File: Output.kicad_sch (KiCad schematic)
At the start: 15 parts, among them U401 74ACT157

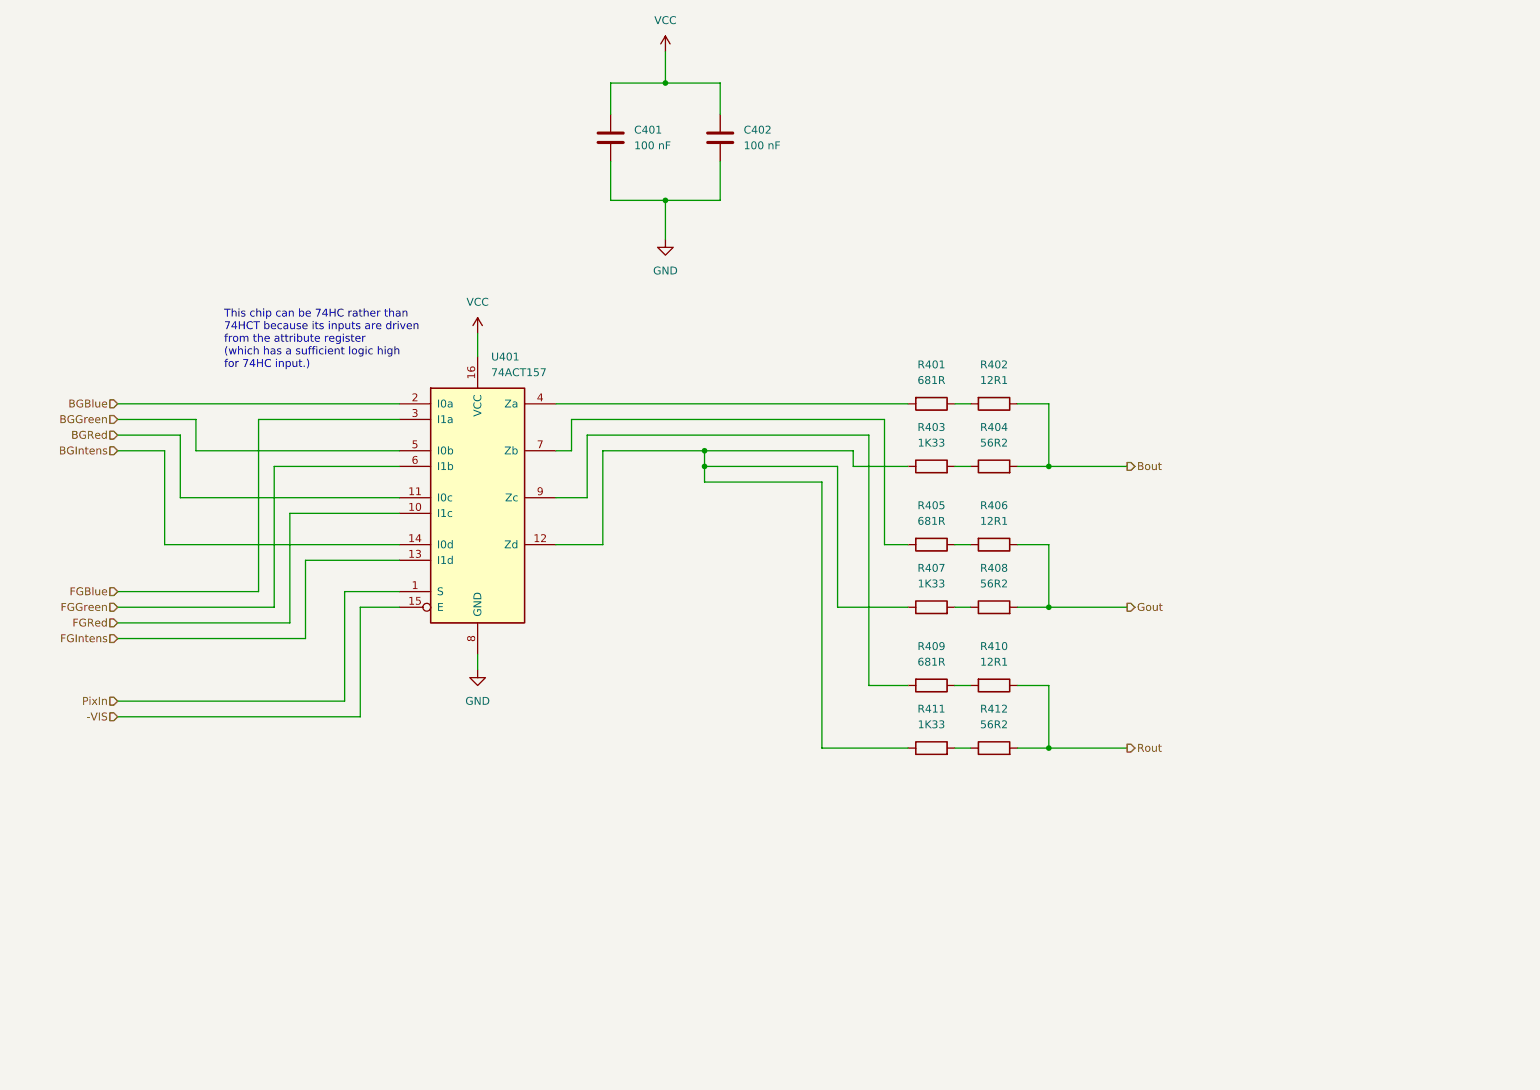
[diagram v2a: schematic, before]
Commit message: minor tweaks to Output circuit
The multiplexor definitely needs to be 74ACT.

Tweaked DAC resistor values to be ones that are more likely
I actually have. (I don't have any 1.33K, for example.)
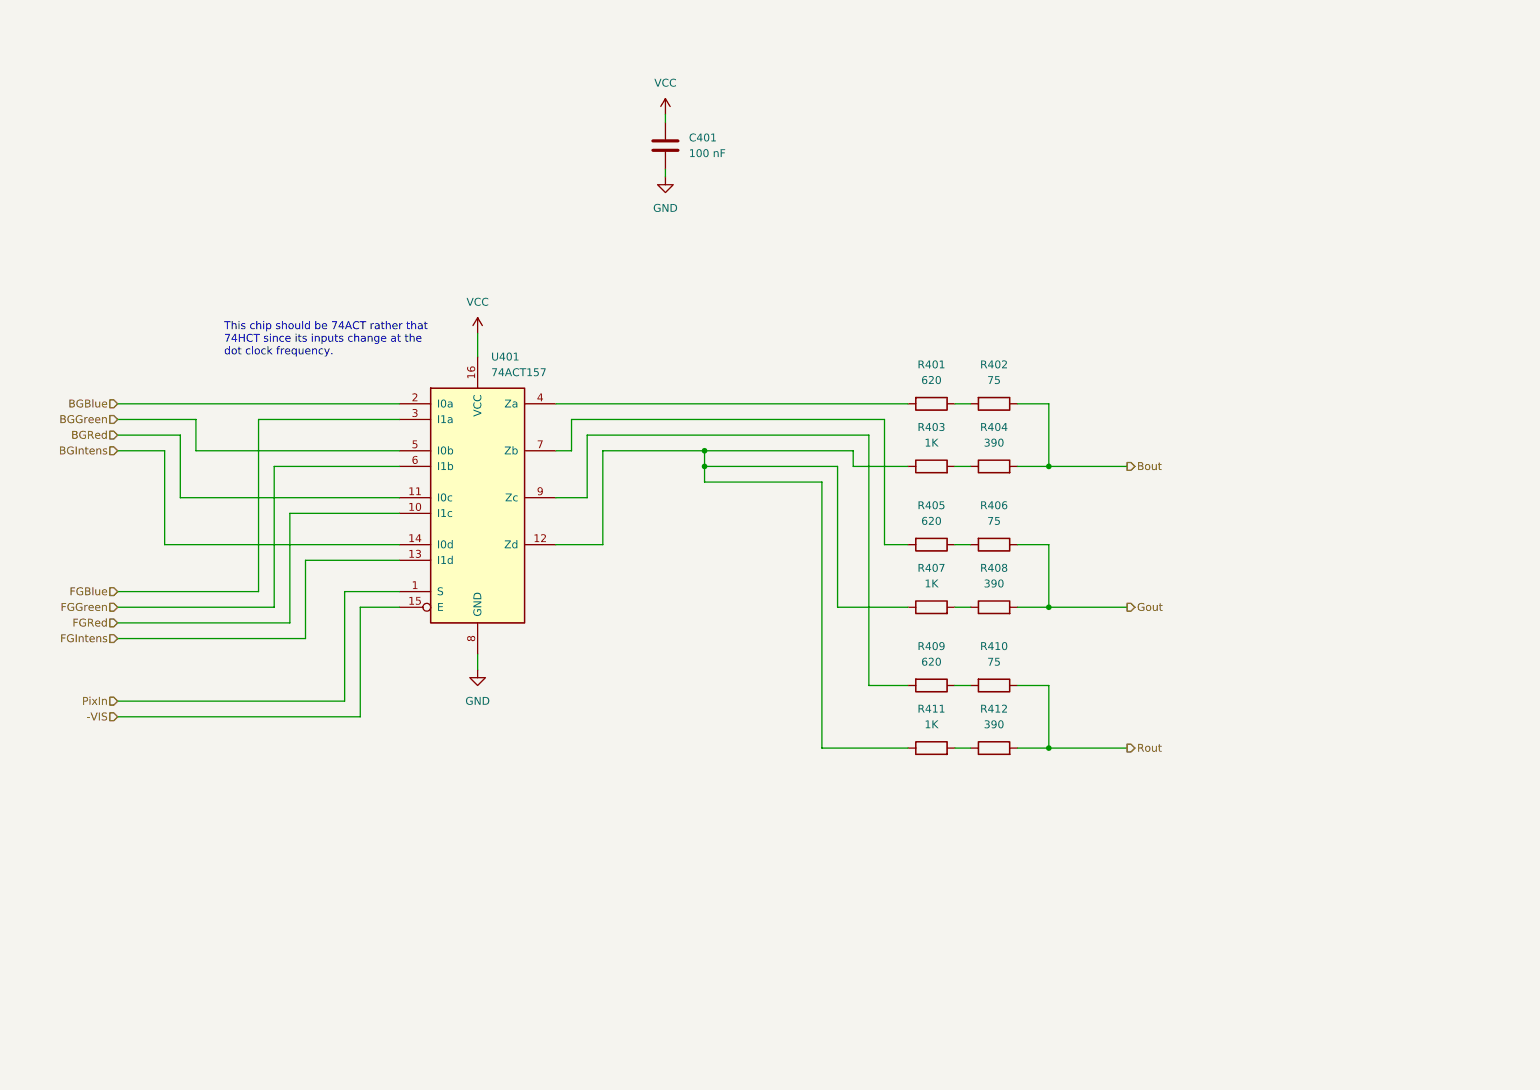
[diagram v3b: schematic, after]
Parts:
- removed C402: 100 nF, symbol Device:C
- R401, R405, R409: value 681R -> 620
- R402, R406, R410: value 12R1 -> 75
- R403, R407, R411: value 1K33 -> 1K
- R404, R408, R412: value 56R2 -> 390
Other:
- note added: "This chip should be 74ACT rather that 74HCT since its inputs change at the dot clock frequency."
- note removed: "This chip can be 74HC rather than 74HCT because its inputs are driven from the attribute register (which has a sufficient logic high for 74HC input.)"
- moved on the sheet: C401
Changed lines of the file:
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@@
-	)
-	(junction
-		(at 128.27 29.21)
-		(diameter 0)
-		(color 0 0 0 0)
 	)
 	(junction
@@
 	)
 	(junction
-		(at 128.27 48.26)
-		(diameter 0)
-		(color 0 0 0 0)
-	)
-	(junction
 		(at 134.62 88.9)
 		(diameter 0)
@@
 	(wire
 		(pts
-			(xy 119.38 41.91) (xy 119.38 48.26)
+			(xy 128.27 43.18) (xy 128.27 44.45)
 		)
 		(stroke
@@
 	(wire
 		(pts
-			(xy 128.27 48.26) (xy 128.27 54.61)
-		)
-		(stroke
-			(width 0)
-			(type default)
-		)
-	)
-	(wire
-		(pts
 			(xy 49.53 86.36) (xy 49.53 96.52)
 		)
@@
 	(wire
 		(pts
-			(xy 128.27 24.13) (xy 128.27 29.21)
-		)
-		(stroke
-			(width 0)
-			(type default)
-		)
-	)
-	(wire
-		(pts
 			(xy 113.03 88.9) (xy 113.03 83.82)
 		)
@@
 	(wire
 		(pts
-			(xy 137.16 29.21) (xy 137.16 34.29)
-		)
-		(stroke
-			(width 0)
-			(type default)
-		)
-	)
-	(wire
-		(pts
-			(xy 119.38 48.26) (xy 128.27 48.26)
-		)
-		(stroke
-			(width 0)
-			(type default)
-		)
-	)
-	(wire
-		(pts
 			(xy 39.37 86.36) (xy 49.53 86.36)
 		)
@@
 	(wire
 		(pts
-			(xy 119.38 29.21) (xy 128.27 29.21)
-		)
-		(stroke
-			(width 0)
-			(type default)
-		)
-	)
-	(wire
-		(pts
 			(xy 156.21 114.3) (xy 156.21 91.44)
 		)
@@
 	(wire
 		(pts
-			(xy 128.27 29.21) (xy 137.16 29.21)
-		)
-		(stroke
-			(width 0)
-			(type default)
-		)
-	)
-	(wire
-		(pts
 			(xy 64.77 114.3) (xy 64.77 91.44)
 		)
@@
 	(wire
 		(pts
-			(xy 128.27 48.26) (xy 137.16 48.26)
-		)
-		(stroke
-			(width 0)
-			(type default)
-		)
-	)
-	(wire
-		(pts
 			(xy 167.64 114.3) (xy 156.21 114.3)
 		)
@@
 	(wire
 		(pts
-			(xy 137.16 48.26) (xy 137.16 41.91)
-		)
-		(stroke
-			(width 0)
-			(type default)
-		)
-	)
-	(wire
-		(pts
-			(xy 119.38 34.29) (xy 119.38 29.21)
+			(xy 128.27 34.29) (xy 128.27 35.56)
 		)
 		(stroke
@@
 		)
 	)
-	(text "This chip can be 74HC rather than\n74HCT because its inputs are driven\nfrom the attribute register\n(which has a sufficient logic high\nfor 74HC input.)"
+	(text "This chip should be 74ACT rather that\n74HCT since its inputs change at the\ndot clock frequency."
 		(exclude_from_sim no)
 		(at 56.642 70.866 0)
@@
 			)
 		)
-		(property "Value" "681R"
+		(property "Value" "620"
 			(at 171.45 100.33 90)
 			(effects
@@
 			)
 		)
-		(property "Value" "1K33"
+		(property "Value" "1K"
 			(at 171.45 110.49 90)
 			(effects
@@
 	(symbol
 		(lib_id "power:GND")
-		(at 128.27 54.61 0)
+		(at 128.27 44.45 0)
 		(unit 1)
 		(exclude_from_sim no)
@@
 		(fields_autoplaced yes)
 		(property "Reference" "#PWR046"
-			(at 128.27 60.96 0)
+			(at 128.27 50.8 0)
 			(effects
 				(font
@@
 		)
 		(property "Value" "GND"
-			(at 128.27 59.69 0)
+			(at 128.27 49.53 0)
 			(effects
 				(font
@@
 		)
 		(property "Footprint" ""
-			(at 128.27 54.61 0)
+			(at 128.27 44.45 0)
 			(effects
 				(font
@@
 		)
 		(property "Datasheet" ""
-			(at 128.27 54.61 0)
+			(at 128.27 44.45 0)
 			(effects
 				(font
@@
 		)
 		(property "Description" "Power symbol creates a global label with name \"GND\" , ground"
-			(at 128.27 54.61 0)
+			(at 128.27 44.45 0)
 			(effects
 				(font
@@
 			)
 		)
-		(property "Value" "1K33"
+		(property "Value" "1K"
 			(at 171.45 87.63 90)
 			(effects
@@
 			)
 		)
-		(property "Value" "56R2"
+		(property "Value" "390"
 			(at 181.61 110.49 90)
 			(effects
@@
 			)
 		)
-		(property "Value" "681R"
+		(property "Value" "620"
 			(at 171.45 77.47 90)
 			(effects
@@
 	(symbol
 		(lib_id "power:VCC")
-		(at 128.27 24.13 0)
+		(at 128.27 34.29 0)
 		(unit 1)
 		(exclude_from_sim no)
@@
 		(fields_autoplaced yes)
 		(property "Reference" "#PWR045"
-			(at 128.27 27.94 0)
+			(at 128.27 38.1 0)
 			(effects
 				(font
@@
 		)
 		(property "Value" "VCC"
-			(at 128.27 19.05 0)
+			(at 128.27 29.21 0)
 			(effects
 				(font
@@
 		)
 		(property "Footprint" ""
-			(at 128.27 24.13 0)
+			(at 128.27 34.29 0)
 			(effects
 				(font
@@
 		)
 		(property "Datasheet" ""
-			(at 128.27 24.13 0)
+			(at 128.27 34.29 0)
 			(effects
 				(font
@@
 		)
 		(property "Description" "Power symbol creates a global label with name \"VCC\""
-			(at 128.27 24.13 0)
+			(at 128.27 34.29 0)
 			(effects
 				(font
@@
 			)
 		)
-		(property "Value" "12R1"
+		(property "Value" "75"
 			(at 181.61 123.19 90)
 			(effects
@@
 			)
 		)
-		(property "Value" "12R1"
+		(property "Value" "75"
 			(at 181.61 77.47 90)
 			(effects
@@
 			)
 		)
-		(property "Value" "12R1"
+		(property "Value" "75"
 			(at 181.61 100.33 90)
 			(effects
@@
 	(symbol
 		(lib_id "Device:C")
-		(at 119.38 38.1 0)
+		(at 128.27 39.37 0)
 		(unit 1)
 		(exclude_from_sim no)
@@
 		(fields_autoplaced yes)
 		(property "Reference" "C401"
-			(at 123.19 36.8299 0)
+			(at 132.08 38.0999 0)
 			(effects
 				(font
@@
 		)
 		(property "Value" "100 nF"
-			(at 123.19 39.3699 0)
+			(at 132.08 40.6399 0)
 			(effects
 				(font
@@
 		)
 		(property "Footprint" ""
-			(at 120.3452 41.91 0)
+			(at 129.2352 43.18 0)
 			(effects
 				(font
@@
 		)
 		(property "Datasheet" "~"
-			(at 119.38 38.1 0)
+			(at 128.27 39.37 0)
 			(effects
 				(font
@@
 		)
 		(property "Description" "Unpolarized capacitor"
-			(at 119.38 38.1 0)
+			(at 128.27 39.37 0)
 			(effects
 				(font
@@
 	)
 	(symbol
-		(lib_id "Device:C")
-		(at 137.16 38.1 0)
-		(unit 1)
-		(exclude_from_sim no)
-		(in_bom yes)
-		(on_board yes)
-		(dnp no)
-		(fields_autoplaced yes)
-		(property "Reference" "C402"
-			(at 140.97 36.8299 0)
-			(effects
-				(font
-					(size 1.27 1.27)
-				)
-				(justify left)
-			)
-		)
-		(property "Value" "100 nF"
-			(at 140.97 39.3699 0)
-			(effects
-				(font
-					(size 1.27 1.27)
-				)
-				(justify left)
-			)
-		)
-		(property "Footprint" ""
-			(at 138.1252 41.91 0)
-			(effects
-				(font
-					(size 1.27 1.27)
-				)
-				(hide yes)
-			)
-		)
-		(property "Datasheet" "~"
-			(at 137.16 38.1 0)
-			(effects
-				(font
-					(size 1.27 1.27)
-				)
-				(hide yes)
-			)
-		)
-		(property "Description" "Unpolarized capacitor"
-			(at 137.16 38.1 0)
-			(effects
-				(font
-					(size 1.27 1.27)
-				)
-				(hide yes)
-			)
-		)
-		(pin "2"
-		)
-		(pin "1"
-		)
-		(instances
-			(project "HW_VGA"
-				(path "/c4bd4b39-993a-4195-805f-b4de6fa4aea5/6938dbb6-3e46-4ac6-b400-805c357c7abb"
-					(reference "C402")
-					(unit 1)
-				)
-			)
-		)
-	)
-	(symbol
 		(lib_id "Device:R")
 		(at 171.45 137.16 90)
@@
 			)
 		)
-		(property "Value" "1K33"
+		(property "Value" "1K"
 			(at 171.45 133.35 90)
 			(effects
@@
 			)
 		)
-		(property "Value" "681R"
+		(property "Value" "620"
 			(at 171.45 123.19 90)
 			(effects
@@
 			)
 		)
-		(property "Value" "56R2"
+		(property "Value" "390"
 			(at 181.61 87.63 90)
 			(effects
@@
 			)
 		)
-		(property "Value" "56R2"
+		(property "Value" "390"
 			(at 181.61 133.35 90)
 			(effects

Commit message: update Output circuit to use '574 as output reg
I think it makes sense to have a register for the
color signal output.
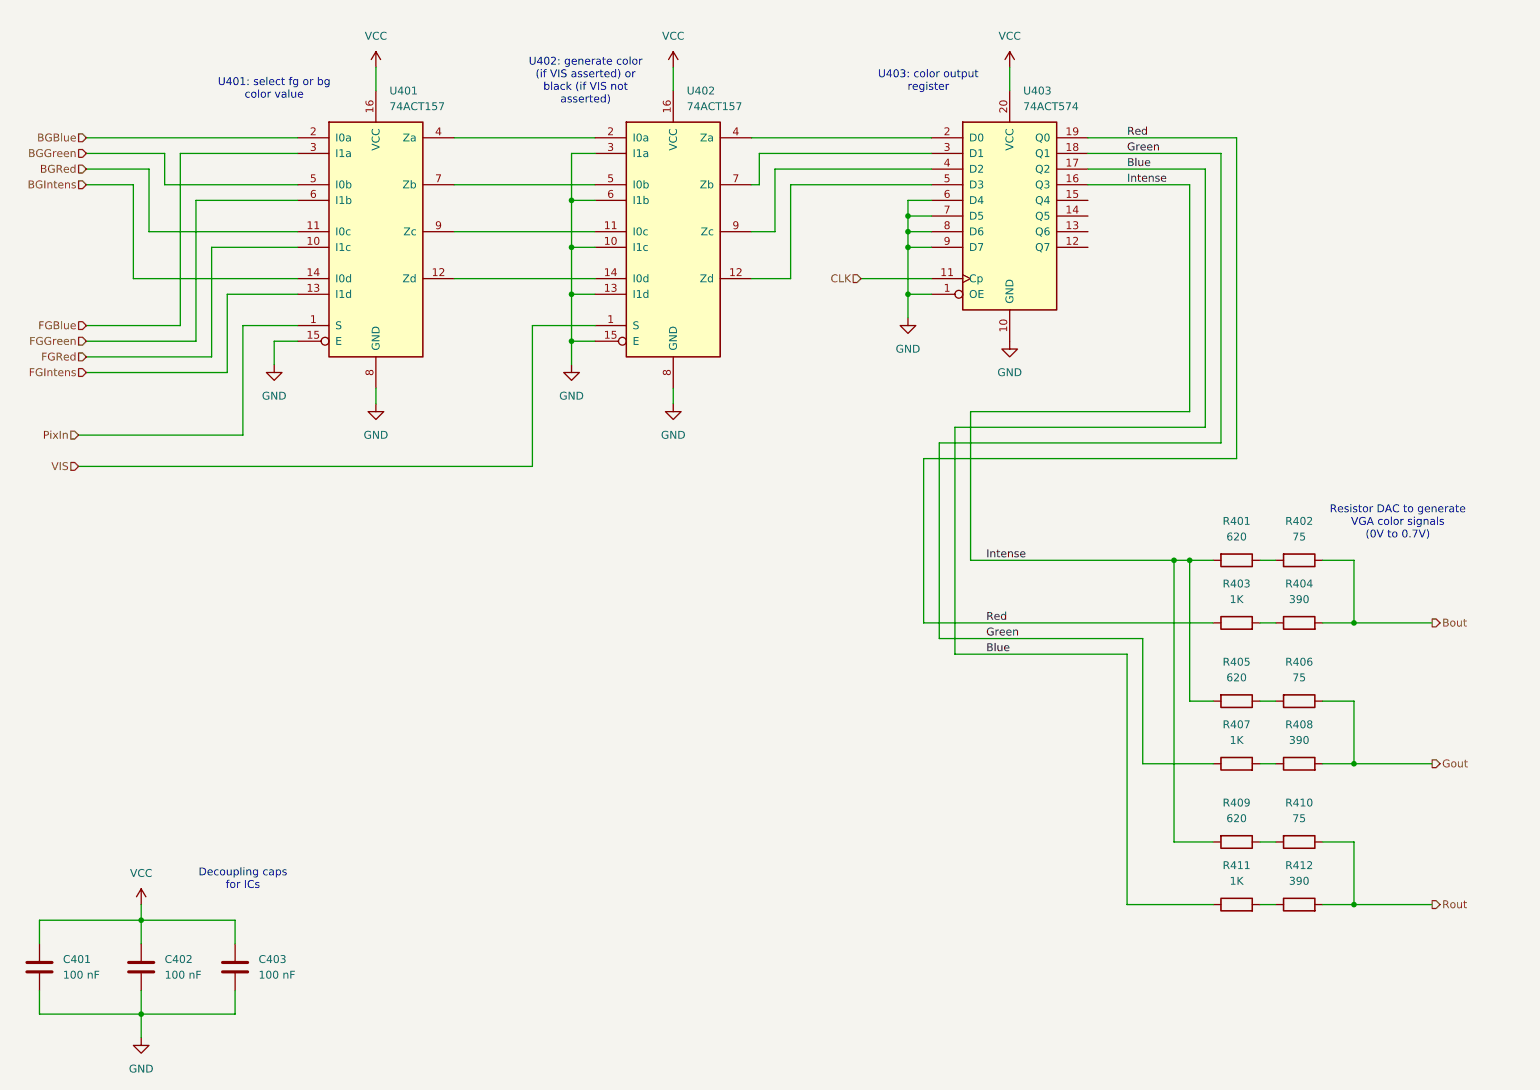
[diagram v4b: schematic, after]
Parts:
- added C402, C403: 100 nF, symbol Device:C
- added U402: 74ACT157, symbol 74xx:74LS157
- added U403: 74ACT574, symbol 74xx:74LS574
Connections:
- net -VIS is gone; now on net GND: U401.15 (E)
- net GND: now also C402.2, C403.2, U402.10 (I1c), U402.13 (I1d), U402.15 (E), U402.3 (I1a), U402.6 (I1b), U402.8 (GND), U403.1 (OE), U403.10 (GND), U403.6 (D4), U403.7 (D5), U403.8 (D6), U403.9 (D7)
- net VCC: now also C402.1, C403.1, U402.16 (VCC), U403.20 (VCC)
- net at U401.7 (Zb): now also U402.5 (I0b); no longer R405.2
- net at U401.4 (Za): now also U402.2 (I0a); no longer R401.2
- net at U401.9 (Zc): now also U402.11 (I0c); no longer R409.2
- new net: U402.4 (Za), U403.2 (D0)
- new net: U402.7 (Zb), U403.3 (D1)
- new net: U402.9 (Zc), U403.4 (D2)
- new net: U402.12 (Zd), U403.5 (D3)
- new net: U401.12 (Zd), U402.14 (I0d)
- new net Blue: R411.1, U403.17 (Q2)
- new net CLK: U403.11 (Cp)
- new net Green: R407.1, U403.18 (Q1)
- new net Intense: R401.2, R405.2, R409.2, U403.16 (Q3)
- new net Red: R403.1, U403.19 (Q0)
- new net VIS: U402.1 (S)
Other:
- note added: "Decoupling caps for ICs"
- note added: "Resistor DAC to generate VGA color signals (0V to 0.7V)"
- note added: "U401: select fg or bg color value"
- note added: "U402: generate color (if VIS asserted) or black (if VIS not asserted)"
- note added: "U403: color output register"
- note removed: "This chip should be 74ACT rather that 74HCT since its inputs change at the dot clock frequency."
- moved on the sheet: C401, R401, R402, R403, R404, R405, R406, R407, R408, R409, R410, R411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

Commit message: make -VIS active-low again
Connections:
- net VIS renamed -VIS
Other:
- note added: "U402: generate color (if -VIS asserted) or black (if -VIS not asserted)"
- note removed: "U402: generate color (if VIS asserted) or black (if VIS not asserted)"
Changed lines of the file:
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@@
 		)
 	)
-	(text "U402: generate color\n(if VIS asserted) or\nblack (if VIS not\nasserted)"
+	(text "U402: generate color\n(if -VIS asserted) or\nblack (if -VIS not\nasserted)"
 		(exclude_from_sim no)
 		(at 115.316 28.956 0)
@@
 		)
 	)
-	(hierarchical_label "VIS"
+	(hierarchical_label "-VIS"
 		(shape input)
 		(at 33.02 91.44 180)
